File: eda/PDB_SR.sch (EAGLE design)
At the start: 14 parts

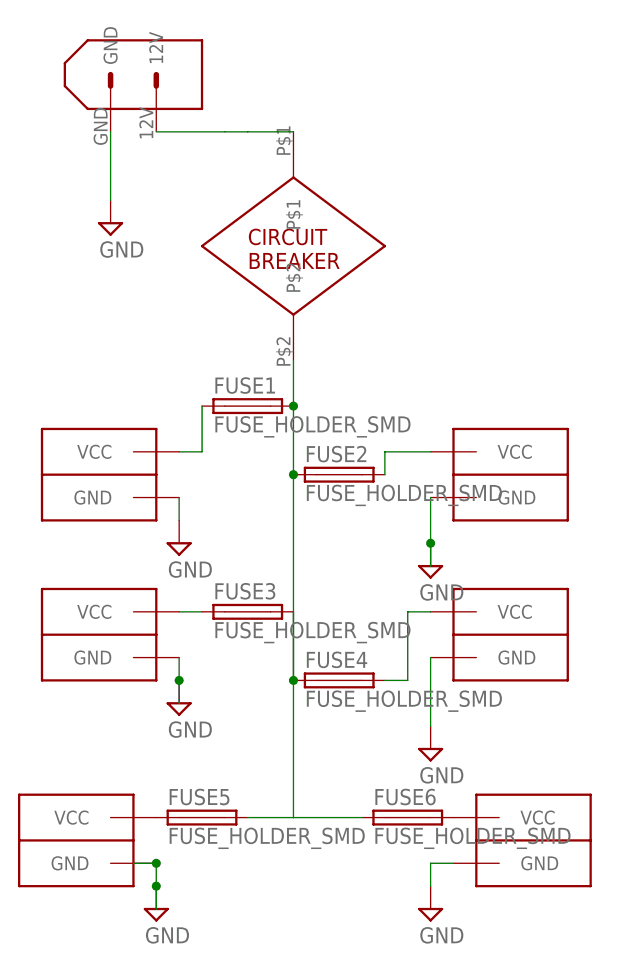
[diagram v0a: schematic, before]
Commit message: Renamed wires from Fuses (N,N, etc) to VOUT_
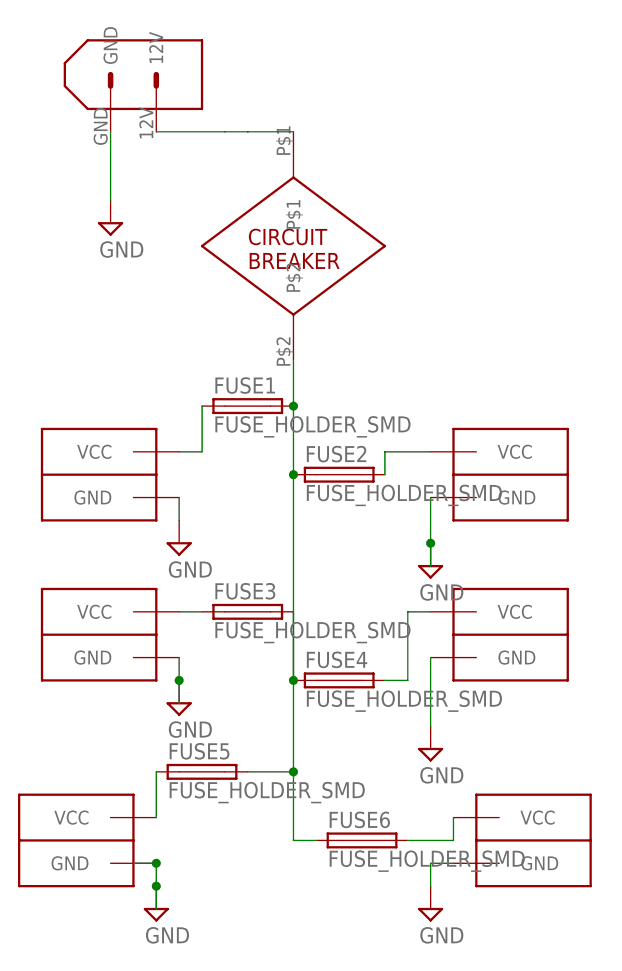
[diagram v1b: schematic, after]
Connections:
- net N$1 renamed VOUT1
- net N$2 renamed VOUT4
- net N$3 renamed VOUT3
- net N$4 renamed VOUT5
- net N$5 renamed VOUT2
- net N$7 renamed VOUT6
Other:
- moved on the sheet: FUSE5, FUSE6
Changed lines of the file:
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@@
 <setting verticaltext="up"/>
 </settings>
-<grid distance="0.1" unitdist="inch" unit="inch" style="lines" multiple="1" display="yes" altdistance="0.01" altunitdist="inch" altunit="inch"/>
+<grid distance="0.1" unitdist="inch" unit="inch" style="lines" multiple="1" display="no" altdistance="0.01" altunitdist="inch" altunit="inch"/>
 <layers>
 <layer number="1" name="Top" color="4" fill="1" visible="no" active="no"/>
@@
 <instance part="FUSE3" gate="G$1" x="25.4" y="50.8"/>
 <instance part="FUSE4" gate="G$1" x="35.56" y="43.18"/>
-<instance part="FUSE5" gate="G$1" x="20.32" y="27.94"/>
-<instance part="FUSE6" gate="G$1" x="43.18" y="27.94"/>
+<instance part="FUSE5" gate="G$1" x="20.32" y="33.02"/>
+<instance part="FUSE6" gate="G$1" x="38.1" y="25.4"/>
 <instance part="CONN3" gate="G$1" x="7.62" y="25.4"/>
 <instance part="CONN6" gate="G$1" x="55.88" y="25.4" rot="MR0"/>
@@
 <wire x1="30.48" y1="43.18" x2="30.48" y2="50.8" width="0.1524" layer="91"/>
 <wire x1="30.48" y1="66.04" x2="30.48" y2="73.66" width="0.1524" layer="91"/>
-<wire x1="30.48" y1="43.18" x2="30.48" y2="27.94" width="0.1524" layer="91"/>
-<wire x1="30.48" y1="27.94" x2="38.1" y2="27.94" width="0.1524" layer="91"/>
-<wire x1="30.48" y1="27.94" x2="25.4" y2="27.94" width="0.1524" layer="91"/>
-<pinref part="FUSE5" gate="G$1" pin="2"/>
-<pinref part="FUSE6" gate="G$1" pin="1"/>
+<wire x1="30.48" y1="43.18" x2="30.48" y2="33.02" width="0.1524" layer="91"/>
 <pinref part="CIRCUIT_BREAKER" gate="G$1" pin="P$2"/>
+<wire x1="30.48" y1="33.02" x2="30.48" y2="25.4" width="0.1524" layer="91"/>
 <wire x1="30.48" y1="78.74" x2="30.48" y2="73.66" width="0.1524" layer="91"/>
 <junction x="30.48" y="73.66"/>
-</segment>
-</net>
-<net name="N$1" class="0">
+<pinref part="FUSE5" gate="G$1" pin="2"/>
+<wire x1="25.4" y1="33.02" x2="30.48" y2="33.02" width="0.1524" layer="91"/>
+<junction x="30.48" y="33.02"/>
+<pinref part="FUSE6" gate="G$1" pin="1"/>
+<wire x1="30.48" y1="25.4" x2="33.02" y2="25.4" width="0.1524" layer="91"/>
+</segment>
+</net>
+<net name="VOUT1" class="0">
 <segment>
 <pinref part="CONN2" gate="G$1" pin="VCC"/>
@@
 </segment>
 </net>
-<net name="N$3" class="0">
+<net name="VOUT3" class="0">
 <segment>
 <pinref part="CONN1" gate="G$1" pin="VCC"/>
@@
 </segment>
 </net>
-<net name="N$5" class="0">
+<net name="VOUT2" class="0">
 <segment>
 <pinref part="CONN4" gate="G$1" pin="VCC"/>
@@
 </segment>
 </net>
-<net name="N$2" class="0">
+<net name="VOUT4" class="0">
 <segment>
 <pinref part="FUSE4" gate="G$1" pin="2"/>
@@
 </segment>
 </net>
-<net name="N$4" class="0">
+<net name="VOUT5" class="0">
 <segment>
 <pinref part="FUSE5" gate="G$1" pin="1"/>
 <pinref part="CONN3" gate="G$1" pin="VCC"/>
-</segment>
-</net>
-<net name="N$7" class="0">
-<segment>
-<pinref part="FUSE6" gate="G$1" pin="2"/>
-<pinref part="CONN6" gate="G$1" pin="VCC"/>
+<wire x1="15.24" y1="33.02" x2="15.24" y2="27.94" width="0.1524" layer="91"/>
 </segment>
 </net>
@@
 </segment>
 </net>
+<net name="VOUT6" class="0">
+<segment>
+<pinref part="FUSE6" gate="G$1" pin="2"/>
+<wire x1="43.18" y1="25.4" x2="48.26" y2="25.4" width="0.1524" layer="91"/>
+<pinref part="CONN6" gate="G$1" pin="VCC"/>
+<wire x1="48.26" y1="25.4" x2="48.26" y2="27.94" width="0.1524" layer="91"/>
+</segment>
+</net>
